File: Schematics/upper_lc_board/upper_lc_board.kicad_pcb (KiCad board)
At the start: 4 copper layers, 69.5 x 60 mm, 121 parts, among them J1 Stack Male Edge Connector, J2 HAL_SENS, J3 PT1, J4 PT2, J5 SOL_CONN, J6 SOL2_CONN, J7 TC, Q1 MOSFET_BSS138, U1 ESP32-S3-WROOM-1-N16R2, U10 OA-TLV9001IDCK, U11 OA-TLV9001IDCK, U12 OA-TLV9001IDCK, U2 CAN_TRX_SN65HVD230DR, U3 PD_D3V3XA4B10LP, U4 PMUX_TPS2121RUXR, U5 TMP117MAIDRVR, U6 TLV75801PDRV, U7 ADC_ADS131M04IPWR, U8 SSR_VO1400AEFTR, U9 OA-TLV9001IDCK

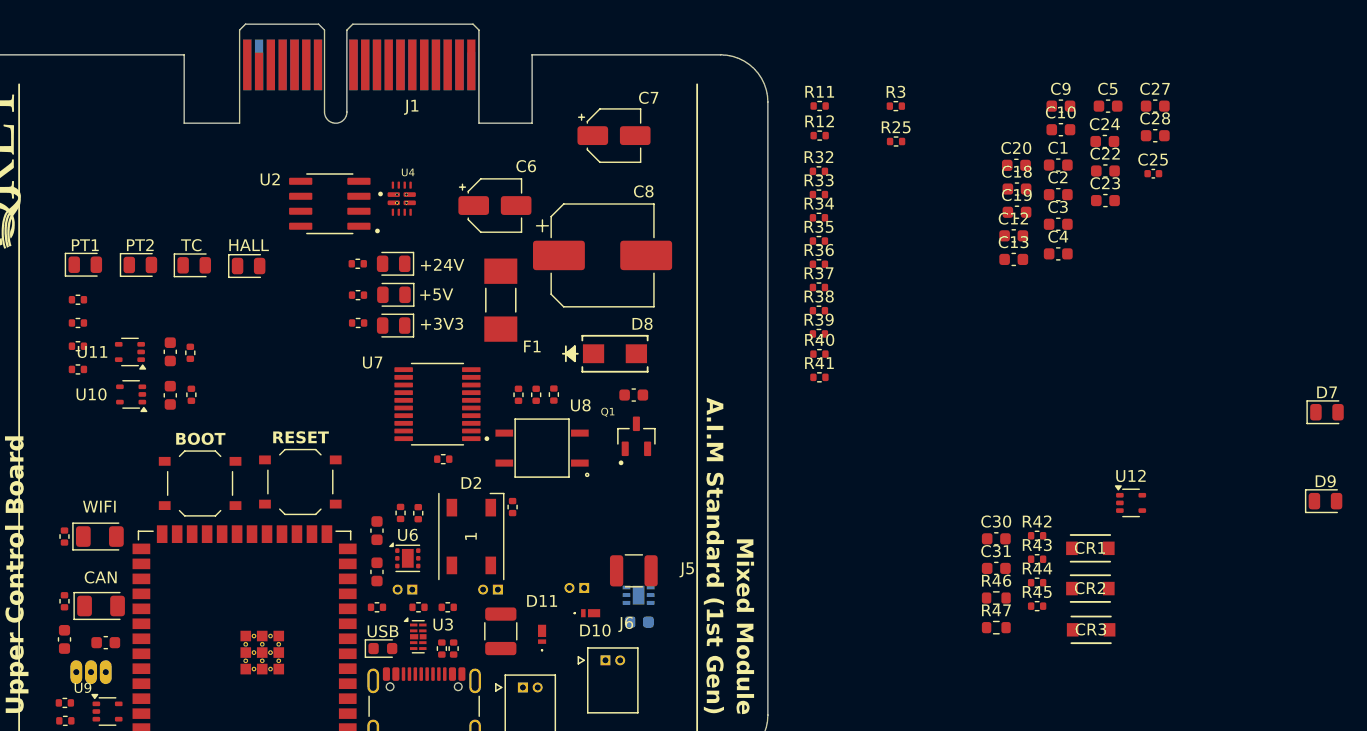
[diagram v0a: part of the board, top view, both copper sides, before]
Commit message: layout work, implement ADC low pass filter layout next
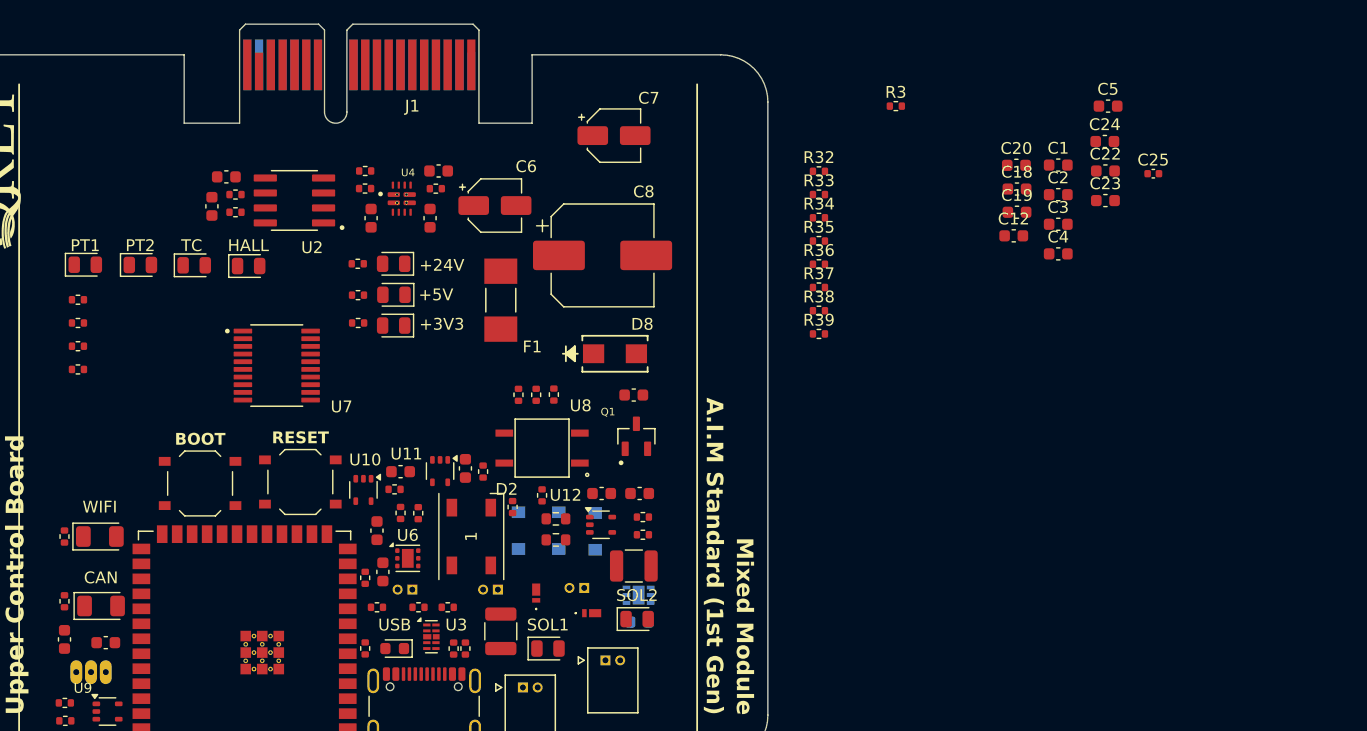
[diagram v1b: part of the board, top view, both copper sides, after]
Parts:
- CR1, CR2, CR3: moved to B.Cu
- moved C28 80.2 mm to (44.5, 33.0), turned to 90 degrees
- moved C27 79.0 mm to (45.7, 30.5)
- moved SOL1 69.0 mm to (73.0, 70.5)
- moved C9 59.3 mm to (58.0, 34.0), turned to 90 degrees
- moved SOL2 59.2 mm to (80.6, 68.0)
- moved R43 57.5 mm to (57.5, 70.5), turned to 90 degrees
- moved R42 57.1 mm to (57.5, 64.5), turned to 90 degrees
- moved C10 54.0 mm to (63.0, 34.0), turned to 90 degrees
- moved R41 51.5 mm to (46.5, 33.5)
- moved R40 51.3 mm to (46.5, 32.0)
- moved C13 49.3 mm to (63.7, 30.0)
- moved CR1 48.5 mm to (70.5, 60.5), turned to -90 degrees
- moved CR2 45.4 mm to (73.9, 60.5), turned to -90 degrees
- moved R25 45.2 mm to (57.5, 31.5)
- moved U12 45.0 mm to (77.5, 60.0)
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- renumbered D7 to SOL1, D9 to SOL2
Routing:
- net CAN_L: track 0.00 -> 0.50 mm

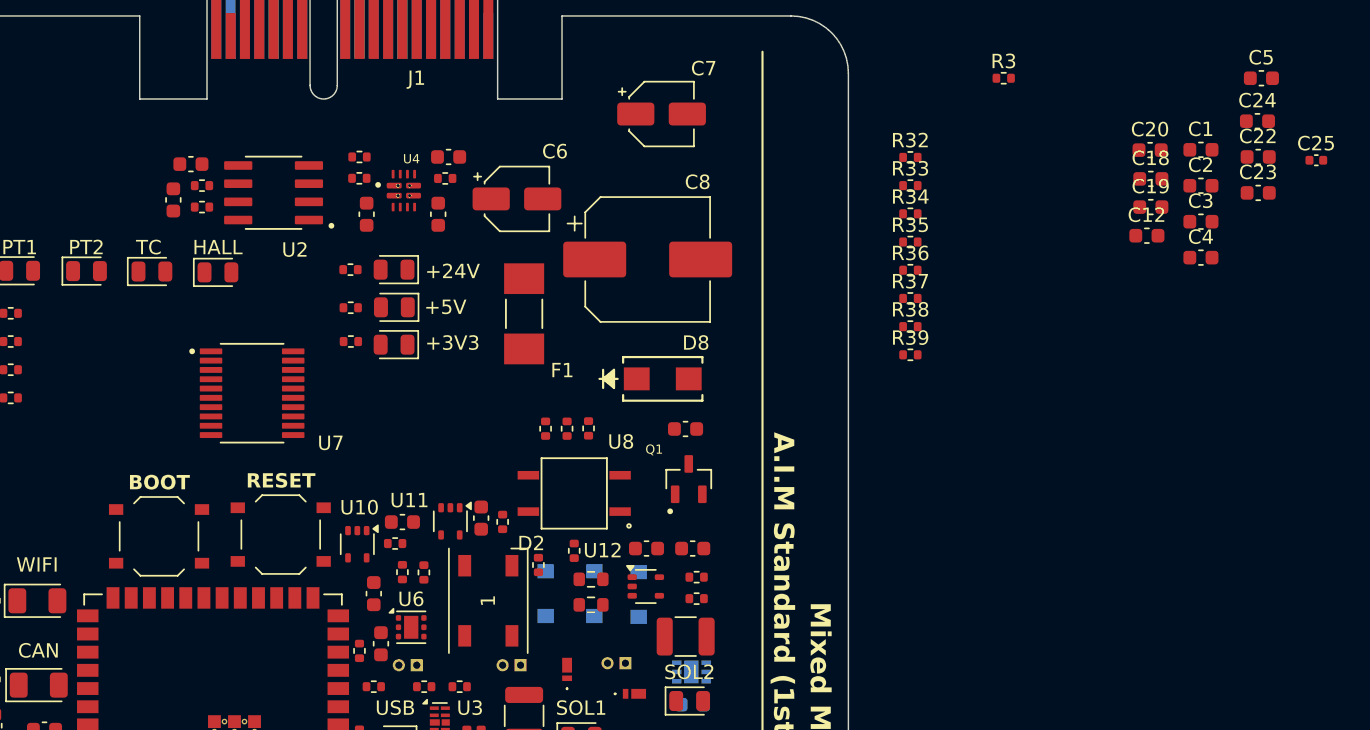
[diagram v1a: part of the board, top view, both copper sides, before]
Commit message: add filter components to layout
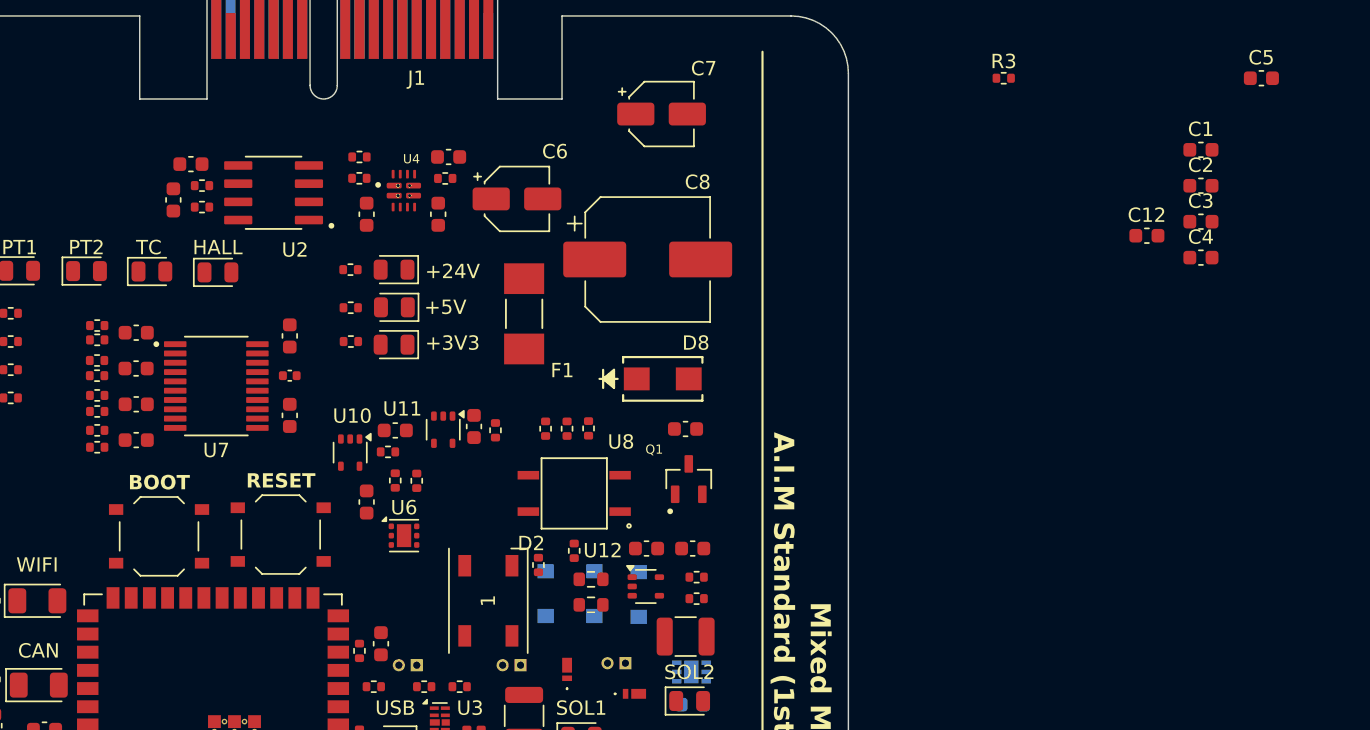
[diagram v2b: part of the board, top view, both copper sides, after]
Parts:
- moved C24 81.4 mm to (41.9, 49.8)
- moved C25 73.3 mm to (52.6, 45.3)
- moved C20 73.0 mm to (41.9, 47.3)
- moved C19 71.8 mm to (41.9, 44.8)
- moved C18 71.7 mm to (41.9, 42.3)
- moved C22 70.0 mm to (52.6, 48.0), turned to 90 degrees
- moved C23 68.4 mm to (52.6, 42.5), turned to 90 degrees
- moved R32 58.0 mm to (39.2, 41.8)
- moved R33 57.8 mm to (39.2, 42.8)
- moved R34 57.7 mm to (39.2, 44.2)
- moved R35 57.6 mm to (39.2, 45.3)
- moved R36 57.5 mm to (39.2, 46.7)
- moved R37 57.3 mm to (39.2, 47.8)
- moved R38 57.3 mm to (39.2, 49.1)
- moved R39 57.2 mm to (39.2, 50.3)
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
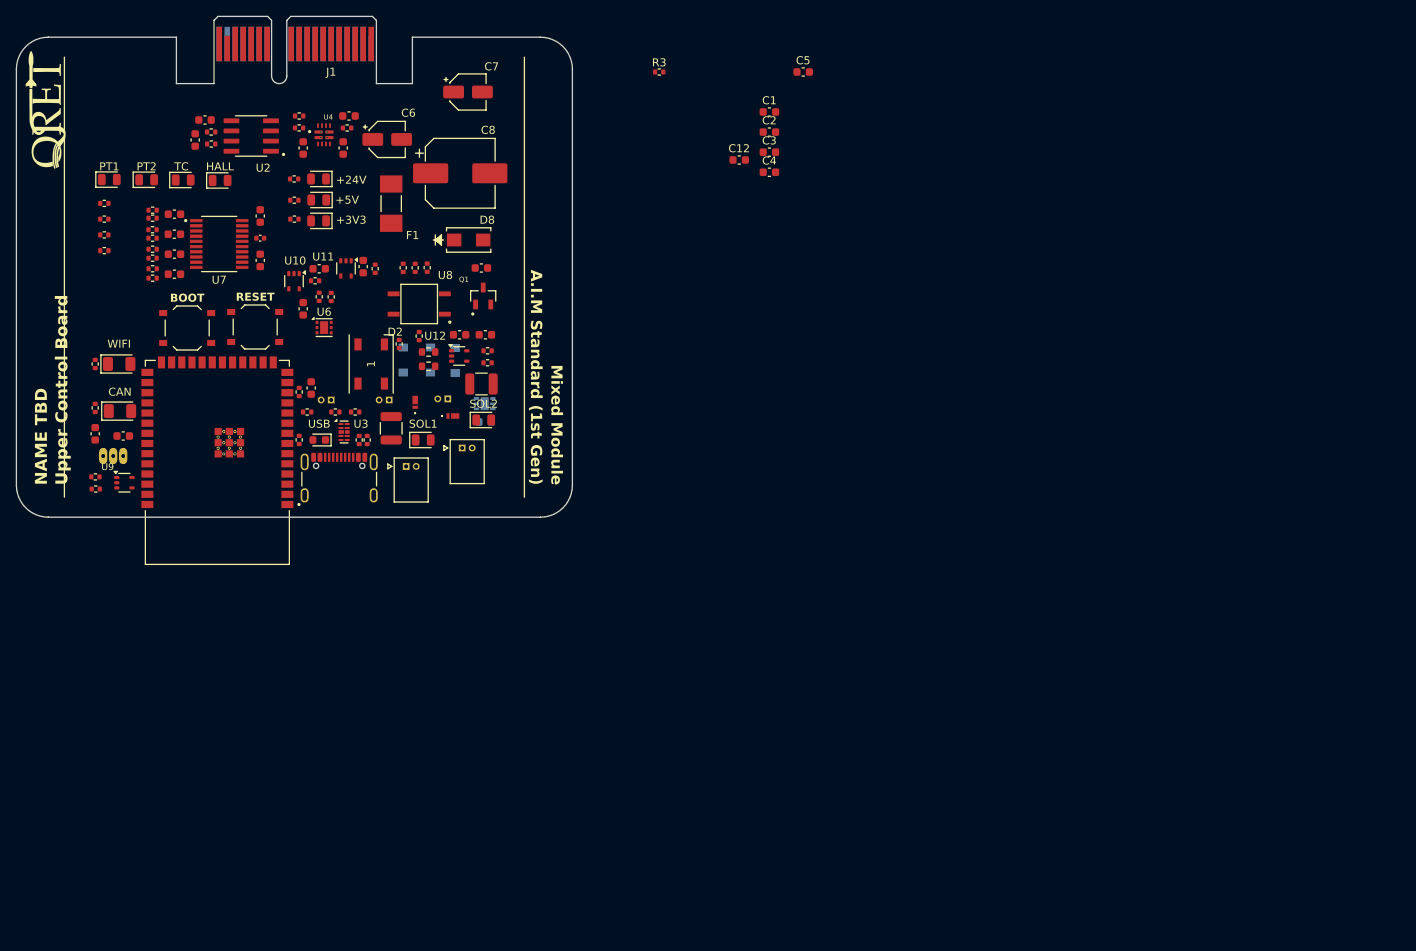
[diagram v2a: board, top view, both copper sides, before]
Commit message: revise & organize some circuitry, next: replace MUX with ideal diodes, finish layout, rename GPIO labels for clarity
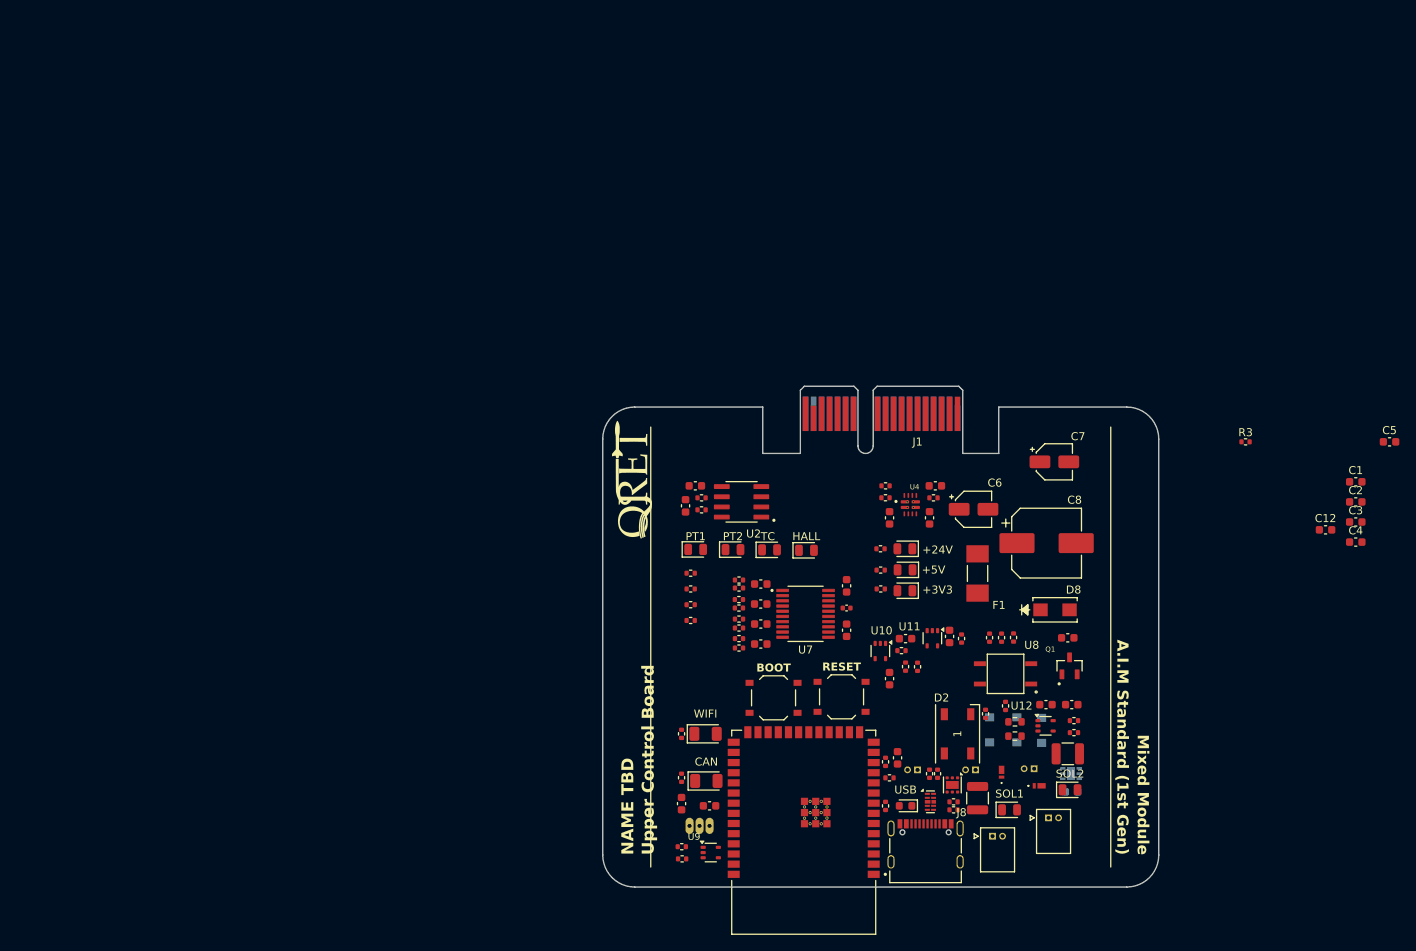
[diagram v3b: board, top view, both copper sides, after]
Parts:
- removed JUSB1: USB_C_CONN_Receptacle_USB2.0, Connector_USB:USB_C_Receptacle_GCT_USB4105-xx-A_16P_TopMnt_Horizontal
- added J8: USB_C_Female_USB2_Small, USBC-CONN:USB_C_DB-108PWB, F.Cu at (135.8, 121.0)
- moved U6 97.1 mm to (139.1, 113.6), turned to -90 degrees
- moved R4 87.5 mm to (139.3, 116.7), turned to 180 degrees
- moved R7 87.0 mm to (136.3, 112.2), turned to 90 degrees
- moved C13 86.7 mm to (137.0, 76.2)
- moved C7 86.7 mm to (151.9, 73.2)
- moved C8 86.7 mm to (150.9, 83.4)
- moved D15 86.7 mm to (111.7, 84.2)
- moved D3 86.7 mm to (133.2, 89.3)
- moved D8 86.7 mm to (152.0, 91.7)
- moved U11 86.7 mm to (136.6, 95.3)
- moved BOOT 86.7 mm to (116.8, 102.7)
- moved C15 86.7 mm to (105.3, 116.0)
- moved C16 86.7 mm to (108.8, 116.2)
- moved C18 86.7 mm to (115.2, 88.5)
- moved C20 86.7 mm to (115.2, 93.5)
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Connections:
- U3 pad 1: /ESP Breakout Cirucitry/USB_N -> /ESP Breakout Cirucitry/USB_D-
- U3 pad 2: /ESP Breakout Cirucitry/USB_P -> /ESP Breakout Cirucitry/USB_D+

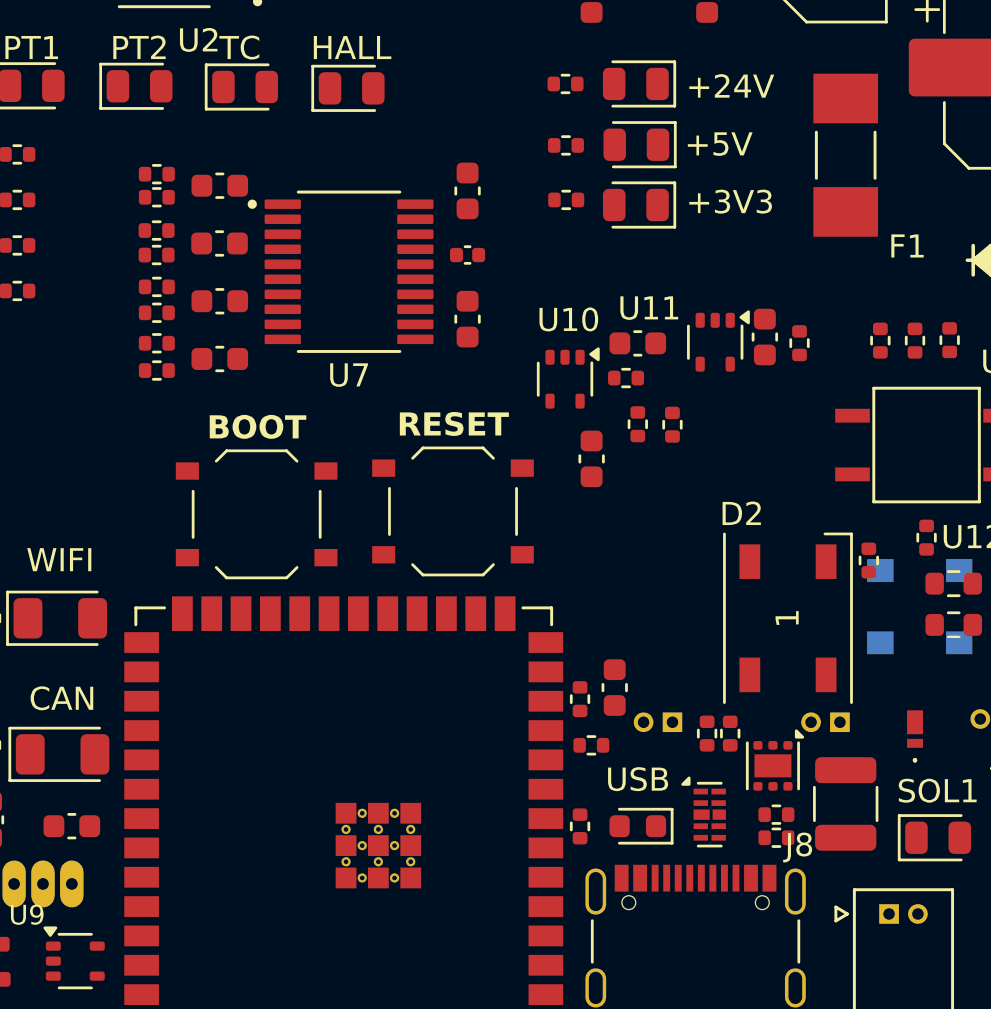
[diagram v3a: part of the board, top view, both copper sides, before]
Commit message: more layout work, add FAULT LED
next: revert to ideal diode circuitry instead of MUX IC.
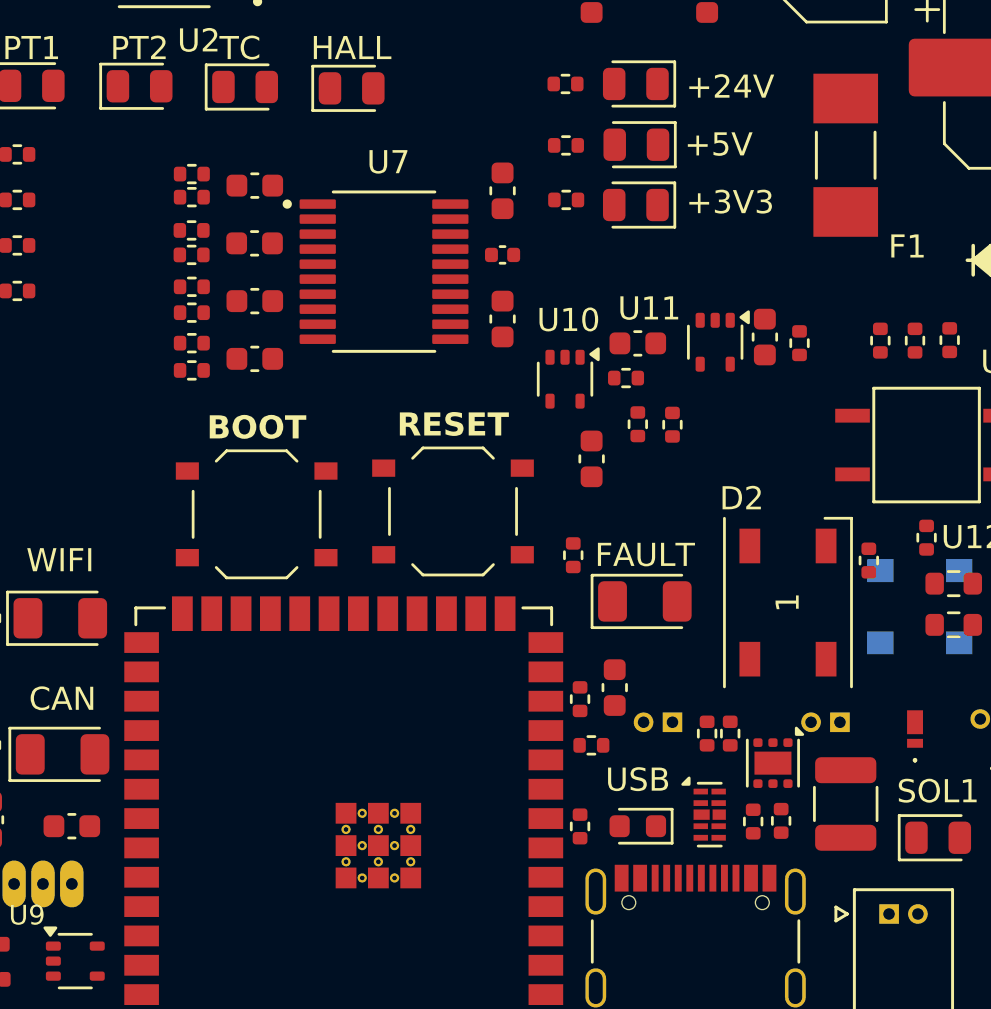
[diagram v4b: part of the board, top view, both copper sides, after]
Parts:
- removed R5: 5.1k, Resistor_SMD:R_0402_1005Metric
- added FAULT: FAULT_LED, LED_SMD:LED_1206_3216Metric, F.Cu at (133.6, 106.5)
- added R48: 5.1k, Resistor_SMD:R_0402_1005Metric, F.Cu at (138.3, 116.0)
- added R49: 5.1k, Resistor_SMD:R_0402_1005Metric, F.Cu at (139.5, 116.0)
- CR1, CR2, CR3: value D_TVS_SMF5.0CA -> D_TVS
- R4: value 5.1k -> 330
- moved R4 15.1 mm to (130.5, 104.5), turned to -90 degrees
- moved C18 1.52 mm to (116.7, 88.5)
- moved C19 1.52 mm to (116.7, 91.0)
- moved C20 1.52 mm to (116.7, 93.5)
- moved C22 1.52 mm to (127.4, 94.3)
- moved C23 1.52 mm to (127.4, 88.7)
- moved C24 1.52 mm to (116.7, 96.0)
- moved C25 1.52 mm to (127.4, 91.5)
- moved R32 1.52 mm to (114.0, 88.0)
- moved R33 1.52 mm to (114.0, 89.0)
- moved R34 1.52 mm to (114.0, 90.4)
- moved R35 1.52 mm to (114.0, 91.5)
- moved R36 1.52 mm to (114.0, 92.9)
- moved R37 1.52 mm to (114.0, 94.0)
- moved R38 1.52 mm to (114.0, 95.3)
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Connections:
- R4 pad 1: Net-(JUSB1-CC1) -> /ESP Breakout Cirucitry/GPIO_3
- R4 pad 2: GND -> Net-(D13-K)
